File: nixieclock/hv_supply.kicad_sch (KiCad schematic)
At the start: 13 parts

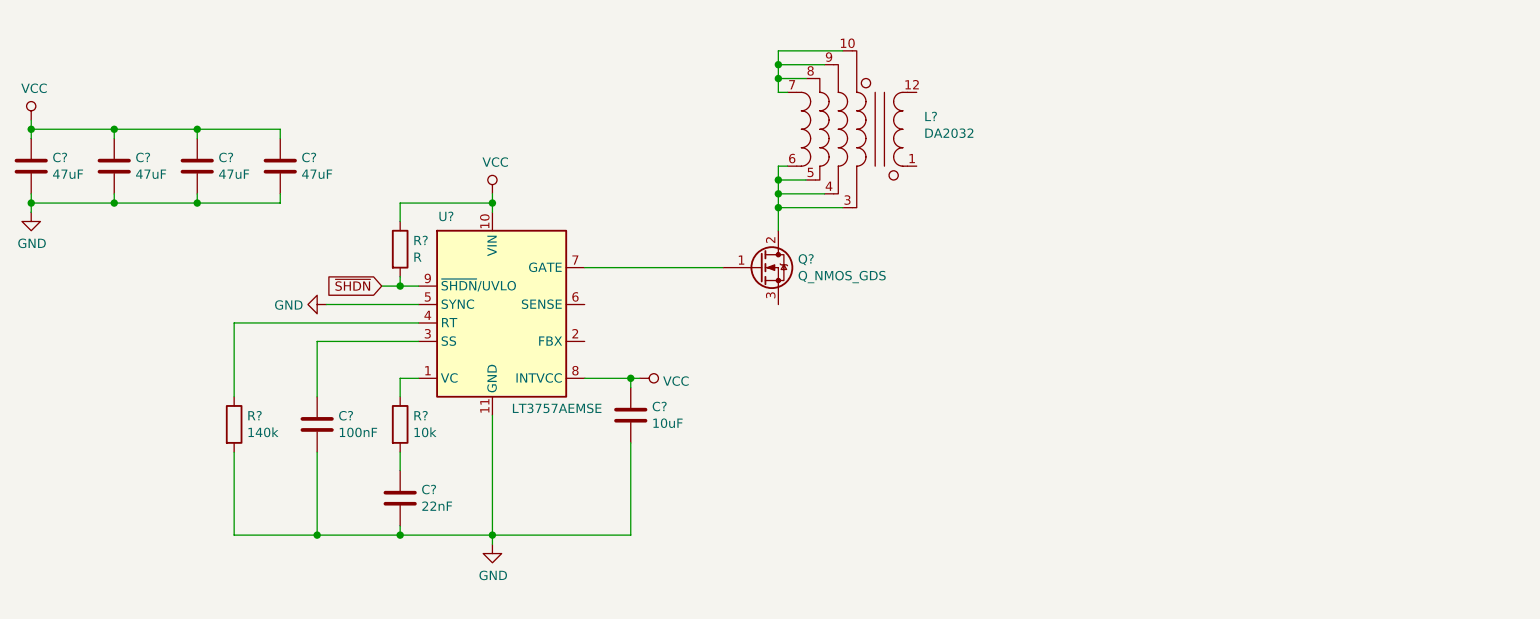
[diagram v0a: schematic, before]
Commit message: Finalized HV supply schematic and assigned footprints
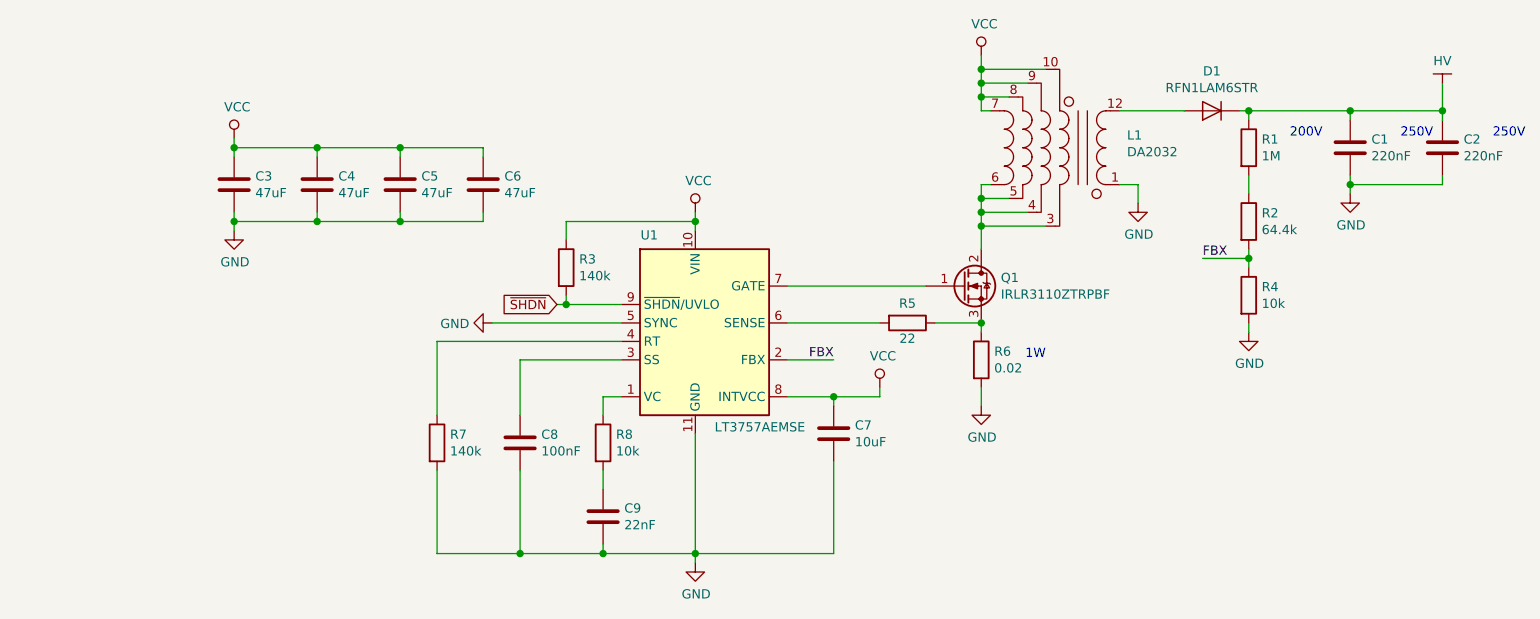
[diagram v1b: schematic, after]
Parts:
- added C1, C2: 220nF, Capacitor_SMD:C_1206_3216Metric_Pad1.42x1.75mm_HandSolder, symbol Device:C
- added D1: RFN1LAM6STR, Personal:SOD128, symbol Device:D
- added R1: 1M, Resistor_SMD:R_1206_3216Metric_Pad1.42x1.75mm_HandSolder, symbol Device:R
- added R2: 64.4k, Resistor_SMD:R_0603_1608Metric_Pad1.05x0.95mm_HandSolder, symbol Device:R
- added R4: 10k, Resistor_SMD:R_0603_1608Metric_Pad1.05x0.95mm_HandSolder, symbol Device:R
- added R5: 22, Resistor_SMD:R_0603_1608Metric_Pad1.05x0.95mm_HandSolder, symbol Device:R
- added R6: 0.02, Resistor_SMD:R_0603_1608Metric_Pad1.05x0.95mm_HandSolder, symbol Device:R
- C3, C4, C5, C6: renamed from C?; footprint (none) -> Capacitor_SMD:C_1210_3225Metric_Pad1.42x2.65mm_HandSolder
- C7, C8, C9: renamed from C?; footprint (none) -> Capacitor_SMD:C_0603_1608Metric_Pad1.05x0.95mm_HandSolder
- L1: renamed from L?; footprint (none) -> Personal:DA2032-AL
- Q1: renamed from Q?; value Q_NMOS_GDS -> IRLR3110ZTRPBF; footprint (none) -> Package_TO_SOT_SMD:TO-252-2
- R3: renamed from R?; value R -> 140k; footprint (none) -> Resistor_SMD:R_0603_1608Metric_Pad1.05x0.95mm_HandSolder
- R7, R8: renamed from R?; footprint (none) -> Resistor_SMD:R_0603_1608Metric_Pad1.05x0.95mm_HandSolder
- gave numbers to parts that had none: 1
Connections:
- net GND: now also L1.1, C1.2, C2.2, R4.2, R6.2
- net VCC: now also L1.10, L1.7, L1.8, L1.9
- net at L1.12: now also D1.2 (A)
- net FBX: now reaches U1.2 (FBX)
- net FBX: now also R2.2, R4.1
- net at U1.6 (SENSE): now also R5.2
- net at Q1.3 (S): now also R5.1, R6.1
- new net: R1.2, R2.1
- new net HV: C1.1, C2.1, D1.1 (K), R1.1
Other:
- note added: "1W"
- note added: "200V"
- note added: "250V"
- moved on the sheet: C3, C4, C5, C6, C7, C8, C9, L1, Q1, R3, R7, R8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
